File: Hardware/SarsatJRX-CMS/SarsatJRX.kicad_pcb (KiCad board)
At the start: 2 copper layers, 65 x 56.5 mm, 38 parts, among them J3 LilyPi GPIO Header, U1 TLC2274, U2 TLC2274

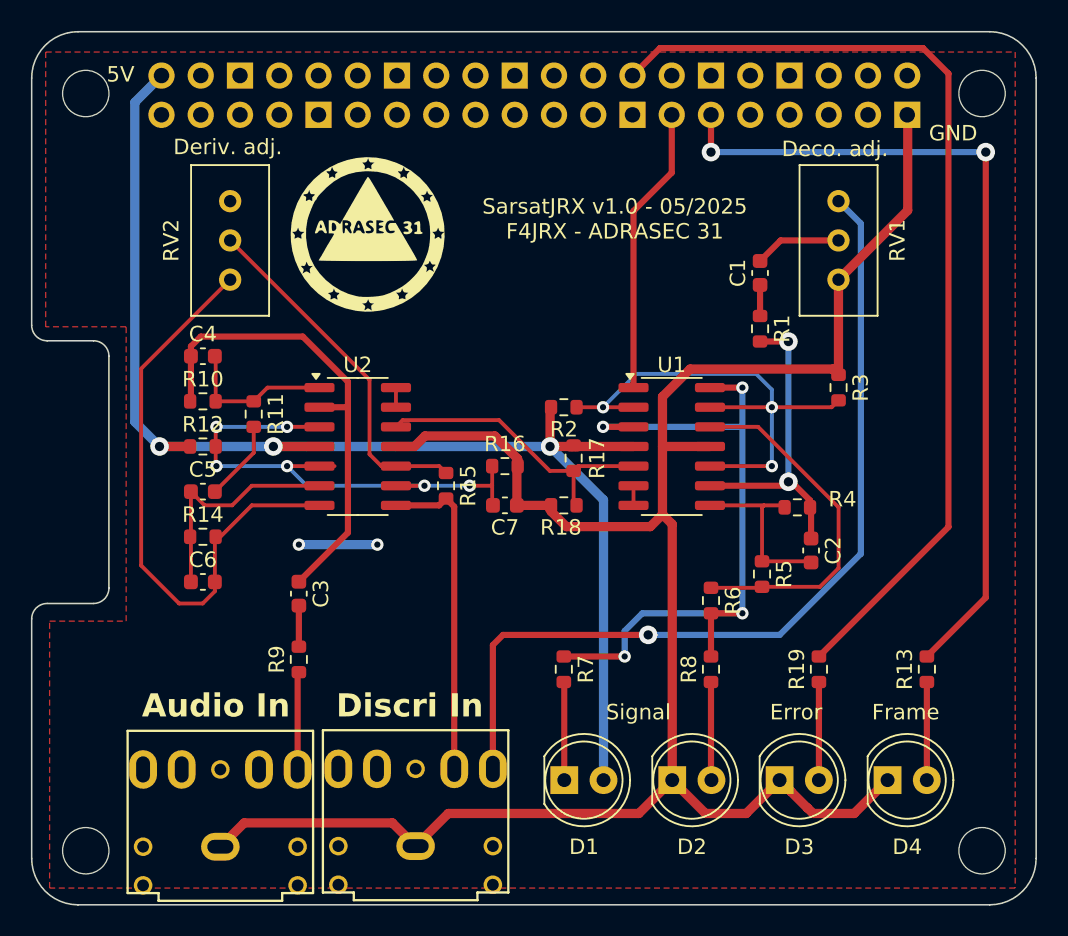
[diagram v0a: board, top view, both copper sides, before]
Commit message: First step to v1.1 of the board : - Added buzzer on IO33 - Mouved led err to IO04 - Added voltage adaptation (5v->3.3v) on Receiver pin (IO25) - Added discri jack insertion detection on IO39 - Added audio input on IO34 - Added decoupling capacitors on 5V power supply for U1 and U2 to try and prevent spikes when wifi is activated - Added ground plane on bottom side of the PCB
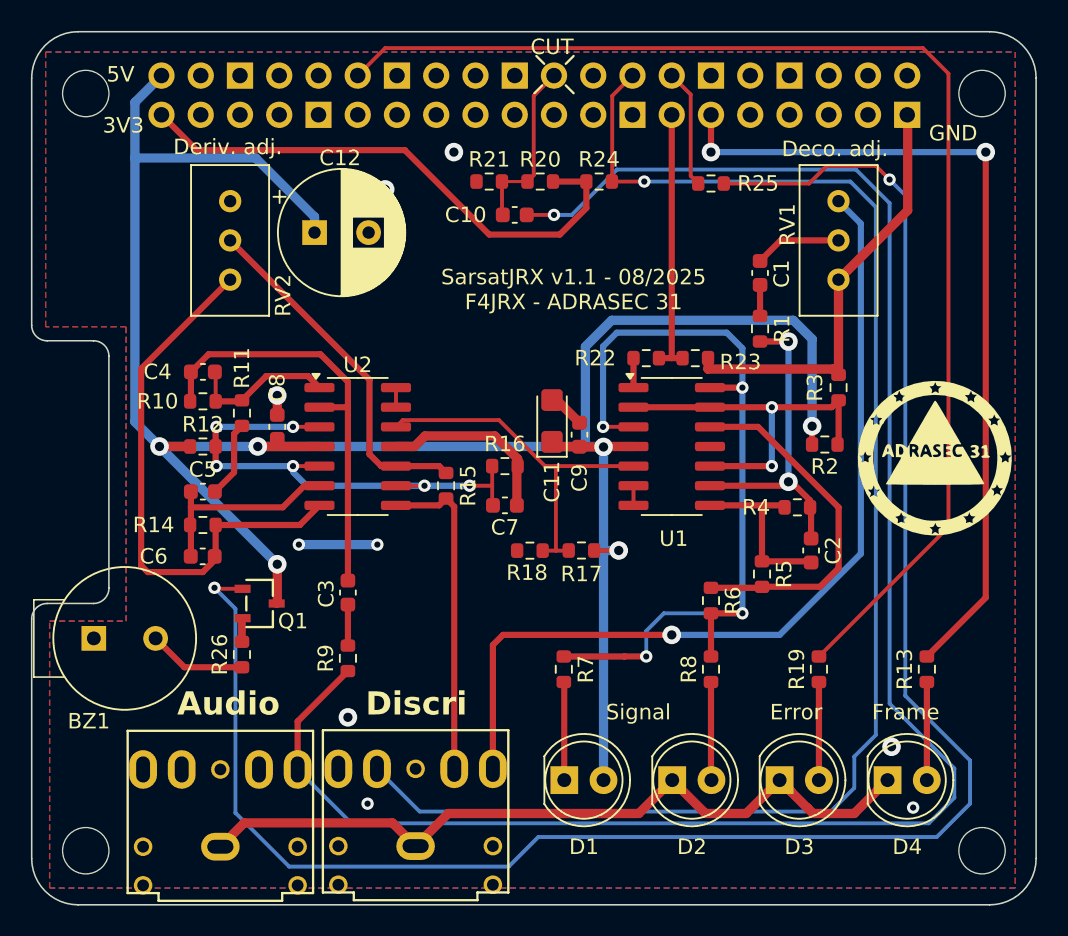
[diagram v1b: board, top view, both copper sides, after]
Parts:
- added BZ1: Buzzer, Buzzer:MagneticBuzzer_PUI_AT-0927-TT-6-R-side-horn, F.Cu at (116.4, 100.4)
- added C10: 100nF, Capacitor_SMD:C_0603_1608Metric, F.Cu at (143.6, 73.0)
- added C11: 10uF, Capacitor_Tantalum_SMD:CP_EIA-3216-18_Kemet-A, F.Cu at (146.0, 86.3)
- added C12: 470uF, Capacitor_THT:CP_Radial_D8.0mm_P3.50mm, F.Cu at (130.7, 74.2)
- added C8: 100nF, Capacitor_SMD:C_0603_1608Metric, F.Cu at (128.2, 86.7)
- added C9: 100nF, Capacitor_SMD:C_0603_1608Metric, F.Cu at (147.8, 87.2)
- added Q1: S8050, j3y:SOT-23-3_L3.0-W1.7-P0.95-LS2.9-BR, F.Cu at (127.1, 98.2)
- added R20: 100K, Resistor_SMD:R_0603_1608Metric, F.Cu at (145.3, 70.8)
- added R21: 100K, Resistor_SMD:R_0603_1608Metric, F.Cu at (142.0, 70.8)
- added R22: 1k, Resistor_SMD:R_0603_1608Metric, F.Cu at (152.1, 82.3)
- added R23: 2k, Resistor_SMD:R_0603_1608Metric, F.Cu at (155.3, 82.3)
- added R24: 10K, Resistor_SMD:R_0603_1608Metric, F.Cu at (149.1, 70.8)
- added R25: 51, Resistor_SMD:R_0603_1608Metric, F.Cu at (156.3, 71.0)
- added R26: 0, Resistor_SMD:R_0603_1608Metric, F.Cu at (126.0, 101.5)
- moved G*** 39.5 mm to (170.8, 88.8)
- moved R2 17.1 mm to (163.7, 87.9)
- moved R17 6.00 mm to (147.9, 94.7), turned to 0 degrees
- moved R18 3.66 mm to (144.6, 94.7)
- moved R9 3.18 mm to (132.8, 101.7)
- moved C3 3.18 mm to (132.8, 97.4)
- moved C6 1.65 mm to (123.4, 95.1)
- moved C4 1.02 mm to (123.4, 83.2)
- moved R11 0.76 mm to (126.0, 85.8)
- moved R14 0.76 mm to (123.4, 93.1)
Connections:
- HEADPHONES2 pad R: unconnected-(HEADPHONES2-PadR) -> GND
- HEADPHONES2 pad RN: unconnected-(HEADPHONES2-PadRN) -> Net-(J3-IO39)
- J3 pad 1: unconnected-(J3-+3v3-Pad1) -> +3.3V
- J3 pad 12: unconnected-(J3-IO4-Pad12) -> Net-(J3-IO4)
- J3 pad 22: unconnected-(J3-IO34-Pad22) -> Net-(J3-IO34)
- J3 pad 28: unconnected-(J3-IO33-Pad28) -> Net-(J3-IO33)
- R19 pad 2: Net-(J3-IO39) -> Net-(J3-IO4)
- U1 pad 1: Net-(J3-IO25) -> Net-(R22-Pad2)
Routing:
- net Net-(Q1-B): track 0.00 -> 121.8 mm, vias 0 -> 2
- net Net-(C10-Pad2): track 6.33 -> 118.2 mm, vias 0 -> 1
- net Net-(J3-IO4): track 0.00 -> 80.8 mm
- net +5V: track 86.6 -> 146.9 mm, vias 3 -> 6
- net GND: track 136.4 -> 98.3 mm, vias 2 -> 10
- net +3.3V: track 0.00 -> 35.3 mm
- net Net-(J3-IO39): track 63.1 -> 96.1 mm, vias 0 -> 1
- net Net-(J3-IO25): track 18.7 -> 0.00 mm
- net Net-(J3-IO34): track 0.00 -> 9.75 mm
- net Net-(U1A--): track 33.4 -> 24.2 mm, vias 3 -> 2
- net Net-(U1A-+): track 46.2 -> 54.7 mm
- net Net-(J3-IO33): track 0.00 -> 7.70 mm
- net Net-(BZ1--): track 0.00 -> 6.36 mm
- net Net-(U1B-+): track 19.6 -> 23.9 mm
- net Net-(U2A--): track 31.3 -> 28.0 mm
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- added copper zone on B.Cu, net GND
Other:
- board text added: "3V3"
- board text added: "Audio"
- board text added: "CUT"
- board text added: "Discri"
- board text added: "SarsatJRX v1.1 - 08/2025 F4JRX - ADRASEC 31"
- board text removed: "Audio In"
- board text removed: "Discri In"
- board text removed: "SarsatJRX v1.0 - 05/2025 F4JRX - ADRASEC 31"

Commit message: Added test points.
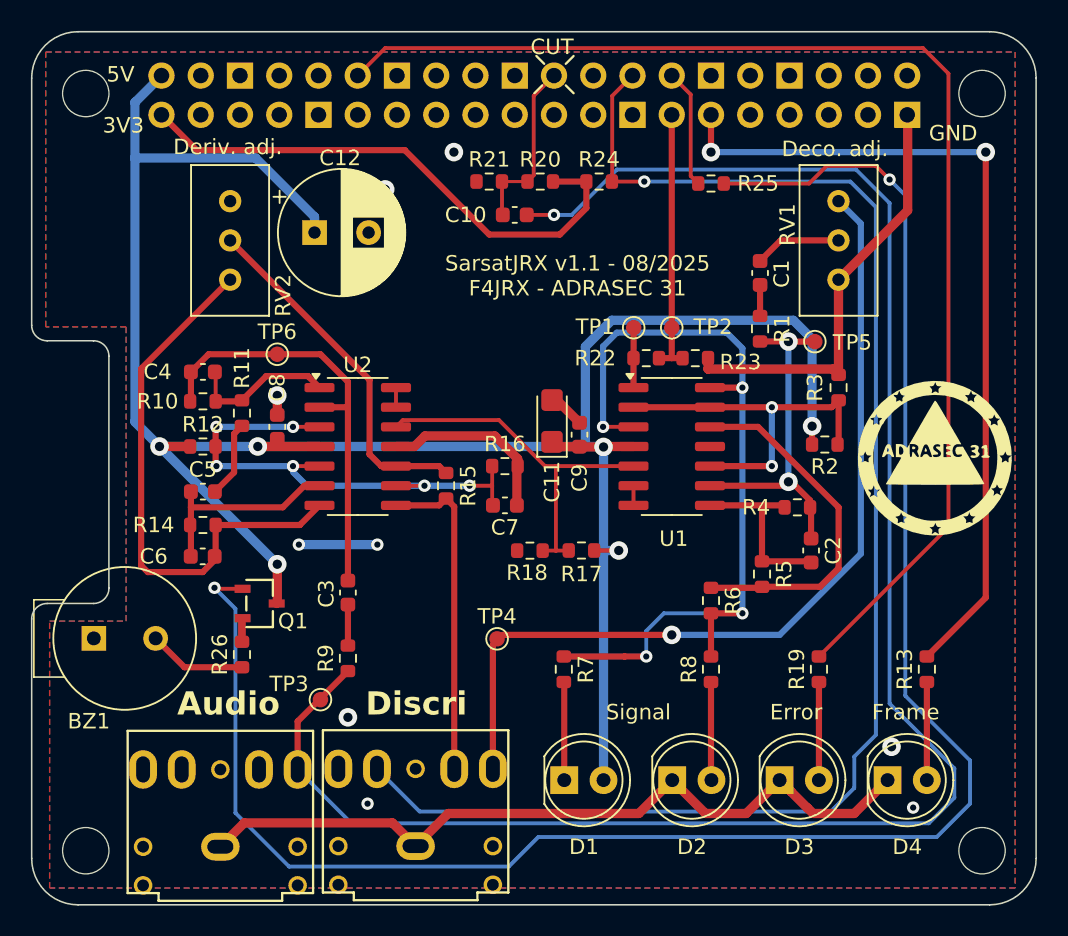
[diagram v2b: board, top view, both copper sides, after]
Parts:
- added TP1: ~, TestPoint:TestPoint_Pad_D1.0mm, F.Cu at (151.3, 80.3)
- added TP2: ~, TestPoint:TestPoint_Pad_D1.0mm, F.Cu at (153.8, 80.3)
- added TP3: ~, TestPoint:TestPoint_Pad_D1.0mm, F.Cu at (131.0, 104.4)
- added TP4: ~, TestPoint:TestPoint_Pad_D1.0mm, F.Cu at (142.5, 100.4)
- added TP5: ~, TestPoint:TestPoint_Pad_D1.0mm, F.Cu at (163.0, 81.2)
- added TP6: ~, TestPoint:TestPoint_Pad_D1.0mm, F.Cu at (128.2, 82.0)
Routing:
- net Net-(U1C--): track 20.5 -> 22.2 mm
